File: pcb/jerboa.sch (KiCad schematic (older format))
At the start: 11 parts, among them P101 SWD_TC, U101 STM32L051K8U6

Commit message: Some schematic work, create a todo with ideas for power supply components
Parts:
- added R?: 1M, agg:0402, symbol agg-kicad:R
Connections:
- net GND: now also R?.2
- net MCU_SHUTDOWN_TO_RADIO: now also R?.1
- net GPS_~RESET: now reaches U101.28 (PB5)
- no-connect marks 17 -> 16
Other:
- moved on the sheet: C101, C102, C103, C104, C105, C106, C107, D101, P101, R101, U101

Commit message: Add TPS61025 switching regulator to schematic
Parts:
- C102, C104, C105, C106, C107: Farnell 2496810 -> 1288282
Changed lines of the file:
@@
 F 2 "agg:0402" H 4250 2200 50  0001 C CNN
 F 3 "" H 4250 2200 50  0001 C CNN
-F 4 "2496810" H 4250 2200 60  0001 C CNN "Farnell"
+F 4 "1288282" H 4250 2200 60  0001 C CNN "Farnell"
 	1    4250 2200
 	1    0    0    -1
@@
 F 2 "agg:0402" H 4050 2400 50  0001 C CNN
 F 3 "" H 4050 2400 50  0001 C CNN
-F 4 "2496810" H 4050 2400 60  0001 C CNN "Farnell"
+F 4 "1288282" H 4050 2400 60  0001 C CNN "Farnell"
 	1    4050 2400
 	1    0    0    -1
@@
 F 2 "agg:0402" H 4250 2600 50  0001 C CNN
 F 3 "" H 4250 2600 50  0001 C CNN
-F 4 "2496810" H 4250 2600 60  0001 C CNN "Farnell"
+F 4 "1288282" H 4250 2600 60  0001 C CNN "Farnell"
 	1    4250 2600
 	1    0    0    -1
@@
 F 2 "agg:0402" H 4700 2750 50  0001 C CNN
 F 3 "" H 4700 2750 50  0001 C CNN
-F 4 "2496810" H 4700 2750 60  0001 C CNN "Farnell"
+F 4 "1288282" H 4700 2750 60  0001 C CNN "Farnell"
 	1    4700 2750
 	0    1    1    0
@@
 F 2 "agg:0402" H 5000 5950 50  0001 C CNN
 F 3 "" H 5000 5950 50  0001 C CNN
-F 4 "2496810" H 5000 5950 60  0001 C CNN "Farnell"
+F 4 "1288282" H 5000 5950 60  0001 C CNN "Farnell"
 	1    5000 5950
 	0    -1   -1   0

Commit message: Create some more schematic symbols and footprints
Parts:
- added IC?: SL18860DC, agg:DFN-10-SL18860DC, symbol agg-kicad:SL18860DC
- added Y?: TCXO, Jerboa:2x1.6mm_TCXO, symbol agg-kicad:TCXO
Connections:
- no-connect marks 16 -> 15
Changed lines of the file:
@@
 	4050 2400 4000 2400
 Wire Wire Line
-	4000 2000 4000 2200
+	4000 2000 4000 2850
 Connection ~ 4000 2600
 Wire Wire Line
@@
 	4400 2800 4150 2800
 Wire Wire Line
-	4400 1900 4400 2000
+	4400 1900 4400 2800
 Connection ~ 4400 2600
 Wire Wire Line
@@
 	4400 2300 5000 2300
 Wire Wire Line
-	4150 2400 4400 2400
+	4150 2400 5000 2400
 Wire Wire Line
 	4400 2500 5000 2500
@@
 NRST
 Wire Wire Line
-	4650 2700 4700 2700
+	4650 2700 5000 2700
 Text Label 6850 4800 0    60   ~ 0
 TX_GPS_from_MCU
@@
 Wire Wire Line
 	6700 4900 6850 4900
-NoConn ~ 5000 3100
 NoConn ~ 5000 3200
 NoConn ~ 6700 2300
@@
 NoConn ~ 6700 5100
 Wire Wire Line
-	5000 6000 5400 6000
-Wire Wire Line
-	5000 5800 5400 5800
+	5000 6000 5500 6000
+Wire Wire Line
+	5000 5800 5500 5800
 Text Label 1600 6150 0    60   ~ 0
 MCU_NSS_TO_RADIO
@@
 MCU_nIRQ_TO_RADIO
 Wire Wire Line
-	4000 2600 4000 2800
-Wire Wire Line
-	4000 2400 4000 2600
-Wire Wire Line
-	4000 2200 4000 2400
-Wire Wire Line
-	4000 2800 4000 2850
-Wire Wire Line
-	4400 2600 4400 2800
-Wire Wire Line
-	4400 2200 4400 2300
-Wire Wire Line
-	4400 2000 4400 2200
-Wire Wire Line
-	4400 2300 4400 2400
-Wire Wire Line
-	4400 2400 5000 2400
-Wire Wire Line
-	4400 2400 4400 2500
-Wire Wire Line
-	4400 2500 4400 2600
-Wire Wire Line
-	5400 5800 5500 5800
-Wire Wire Line
-	5400 6000 5500 6000
-Wire Wire Line
-	4700 2700 5000 2700
-Wire Wire Line
 	6850 4800 6700 4800
 $Comp
@@
 	8100 2700 8100 2650
 Wire Wire Line
-	6700 2500 8100 2500
+	6700 2500 8300 2500
 Wire Wire Line
 	8100 2550 8100 2500
 Connection ~ 8100 2500
-Wire Wire Line
-	8100 2500 8300 2500
 Wire Wire Line
 	1400 3700 1600 3700
@@
 Wire Wire Line
 	6850 4700 6700 4700
+$Comp
+L agg-kicad:SL18860DC IC?
+U 1 1 5A7CC280
+P 3250 4450
+F 0 "IC?" H 3250 5075 50  0000 C CNN
+F 1 "SL18860DC" H 3250 4984 50  0000 C CNN
+F 2 "agg:DFN-10-SL18860DC" H 2850 3850 50  0001 L CNN
+F 3 "http://www.silabs.com/Support%20Documents/TechnicalDocs/SL18860.pdf" H 2850 3750 50  0001 L CNN
+F 4 "634-SL18860DC" H 2850 3650 50  0001 L CNN "Mouser"
+	1    3250 4450
+	1    0    0    -1
+$EndComp
+$Comp
+L agg-kicad:TCXO Y?
+U 1 1 5A7E3BDC
+P 2250 4500
+F 0 "Y?" H 2250 4725 50  0000 C CNN
+F 1 "TCXO" H 2250 4634 50  0000 C CNN
+F 2 "Jerboa:2x1.6mm_TCXO" H 2050 4500 50  0001 C CNN
+F 3 "http://www.farnell.com/datasheets/2045487.pdf" H 2050 4500 50  0001 C CNN
+F 4 "2545847" H 2050 4200 50  0001 L CNN "Farnell"
+	1    2250 4500
+	1    0    0    -1
+$EndComp
 $EndSCHEMATC

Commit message: Work on schematic
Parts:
- added C? (x2): 100nF, agg:0402, symbol agg-kicad:C
- added C?: 10uF, agg:0402, symbol agg-kicad:C
- added R? (x2): 10k, symbol agg-kicad:R
- added R?: 50, symbol agg-kicad:R
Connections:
- net 3v3: now also IC?.6 (OE1), IC?.7 (OE2), Y?.4 (VCC), C?.2, R?.1
- net GND: now also IC?.1 (VSS), IC?.5 (OE3), Y?.2 (GND), C?.1, C?.1, C?.1, R?.2
- net MCU_CLK: now reaches U101.2 (PC14-OSC_IN)
- net MCU_CLK: now also IC?.8 (CLKOUT1)
- net at IC?.2 (VDD): now also C?.2, C?.2, R?.2
- net at IC?.3 (CLKIN): now also Y?.3 (OUT)
- net at IC?.9 (CLKOUT2): now also R?.1
- new net SI4460_CLK: R?.1, R?.2
- no-connect marks 15 -> 17
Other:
- note removed: "No DFU required"
- moved on the sheet: C101, C102, C103, C104, C105, C106, C107, D101, IC?, P101, R101, R?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

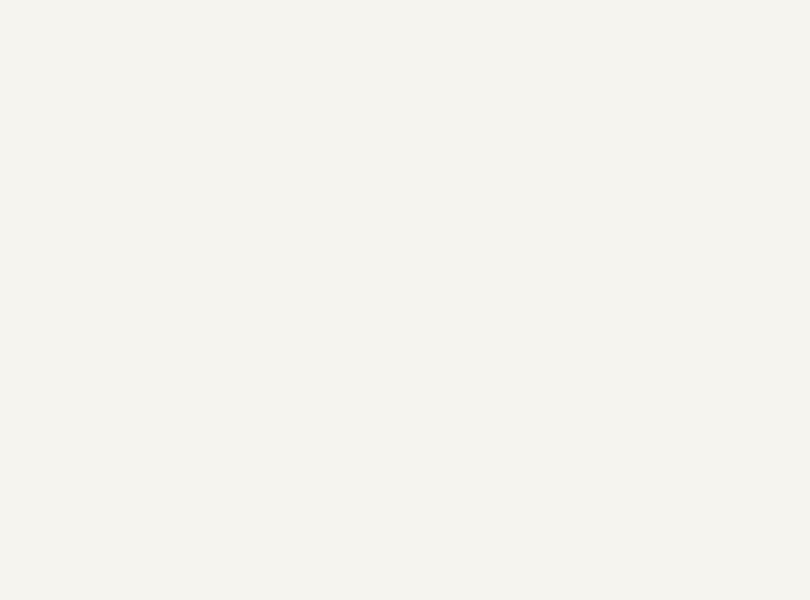
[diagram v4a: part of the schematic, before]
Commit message: Add wspr breakout board and reorganise sub project libraries
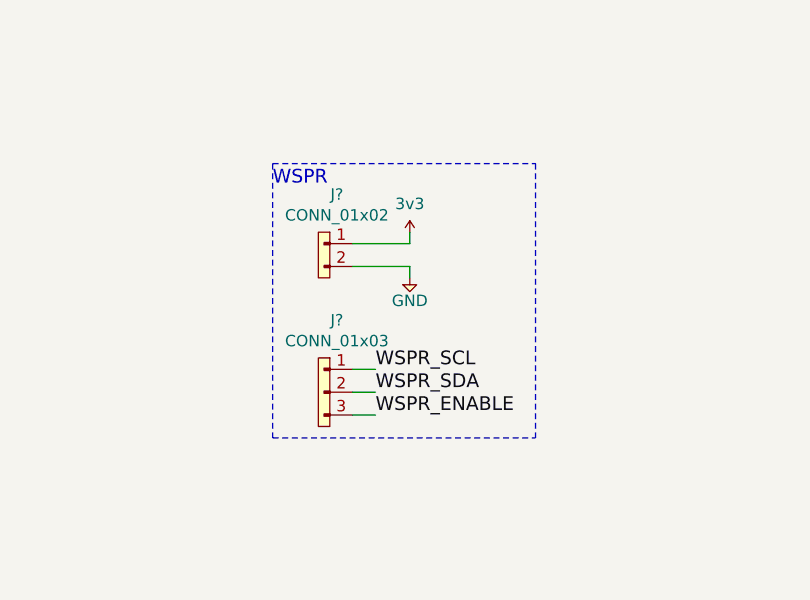
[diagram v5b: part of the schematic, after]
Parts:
- added J?: CONN_01x02, agg:SIL-254P-02, symbol agg-kicad:CONN_01x02
- added J?: CONN_01x03, symbol agg-kicad:CONN_01x03
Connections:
- net 3v3: now also J?.1
- net GND: now also J?.2
- new net WSPR_ENABLE: J?.3
- new net WSPR_SCL: J?.1
- new net WSPR_SDA: J?.2
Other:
- note added: "WSPR"
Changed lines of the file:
@@
 	3350 4100 3350 4050
 Connection ~ 3350 4250
+$Comp
+L agg-kicad:CONN_01x02 J?
+U 1 1 5A89E783
+P 3200 1750
+F 0 "J?" H 3231 1965 50  0000 C CNN
+F 1 "CONN_01x02" H 3231 1874 50  0000 C CNN
+F 2 "agg:SIL-254P-02" H 3200 1750 50  0001 C CNN
+F 3 "http://www.farnell.com/datasheets/2290158.pdf" H 3200 1750 50  0001 C CNN
+F 4 "1593458" H 3200 1750 50  0001 C CNN "Farnell"
+	1    3200 1750
+	1    0    0    -1
+$EndComp
+$Comp
+L agg-kicad:GND #PWR?
+U 1 1 5A89E908
+P 3550 1900
+F 0 "#PWR?" H 3420 1940 50  0001 L CNN
+F 1 "GND" H 3550 1800 50  0000 C CNN
+F 2 "" H 3550 1900 60  0001 C CNN
+F 3 "" H 3550 1900 60  0001 C CNN
+F 4 "Value" H 3550 1900 50  0001 C CNN "Farnell"
+	1    3550 1900
+	1    0    0    -1
+$EndComp
+$Comp
+L agg-kicad:3v3 #PWR?
+U 1 1 5A89EBB4
+P 3550 1700
+F 0 "#PWR?" H 3550 1810 50  0001 L CNN
+F 1 "3v3" H 3550 1824 50  0000 C CNN
+F 2 "" H 3550 1700 60  0001 C CNN
+F 3 "" H 3550 1700 60  0001 C CNN
+	1    3550 1700
+	1    0    0    -1
+$EndComp
+Wire Wire Line
+	3550 1900 3550 1850
+Wire Wire Line
+	3550 1850 3300 1850
+Wire Wire Line
+	3300 1750 3550 1750
+Wire Wire Line
+	3550 1750 3550 1700
+$Comp
+L agg-kicad:CONN_01x03 J?
+U 1 1 5A8A71F9
+P 3200 2300
+F 0 "J?" H 3231 2515 50  0000 C CNN
+F 1 "CONN_01x03" H 3231 2424 50  0000 C CNN
+F 2 "" H 3200 2300 50  0001 C CNN
+F 3 "" H 3200 2300 50  0001 C CNN
+	1    3200 2300
+	1    0    0    -1
+$EndComp
+Text Label 3400 2300 0    60   ~ 0
+WSPR_SCL
+Text Label 3400 2400 0    60   ~ 0
+WSPR_SDA
+Text Label 3400 2500 0    60   ~ 0
+WSPR_ENABLE
+Wire Wire Line
+	3400 2300 3300 2300
+Wire Wire Line
+	3300 2400 3400 2400
+Wire Wire Line
+	3300 2500 3400 2500
+Text Notes 2950 1500 0    60   ~ 0
+WSPR
+Wire Notes Line
+	2950 1400 2950 2600
+Wire Notes Line
+	2950 2600 4100 2600
+Wire Notes Line
+	2950 1400 4100 1400
+Wire Notes Line
+	4100 1400 4100 2600
 $EndSCHEMATC

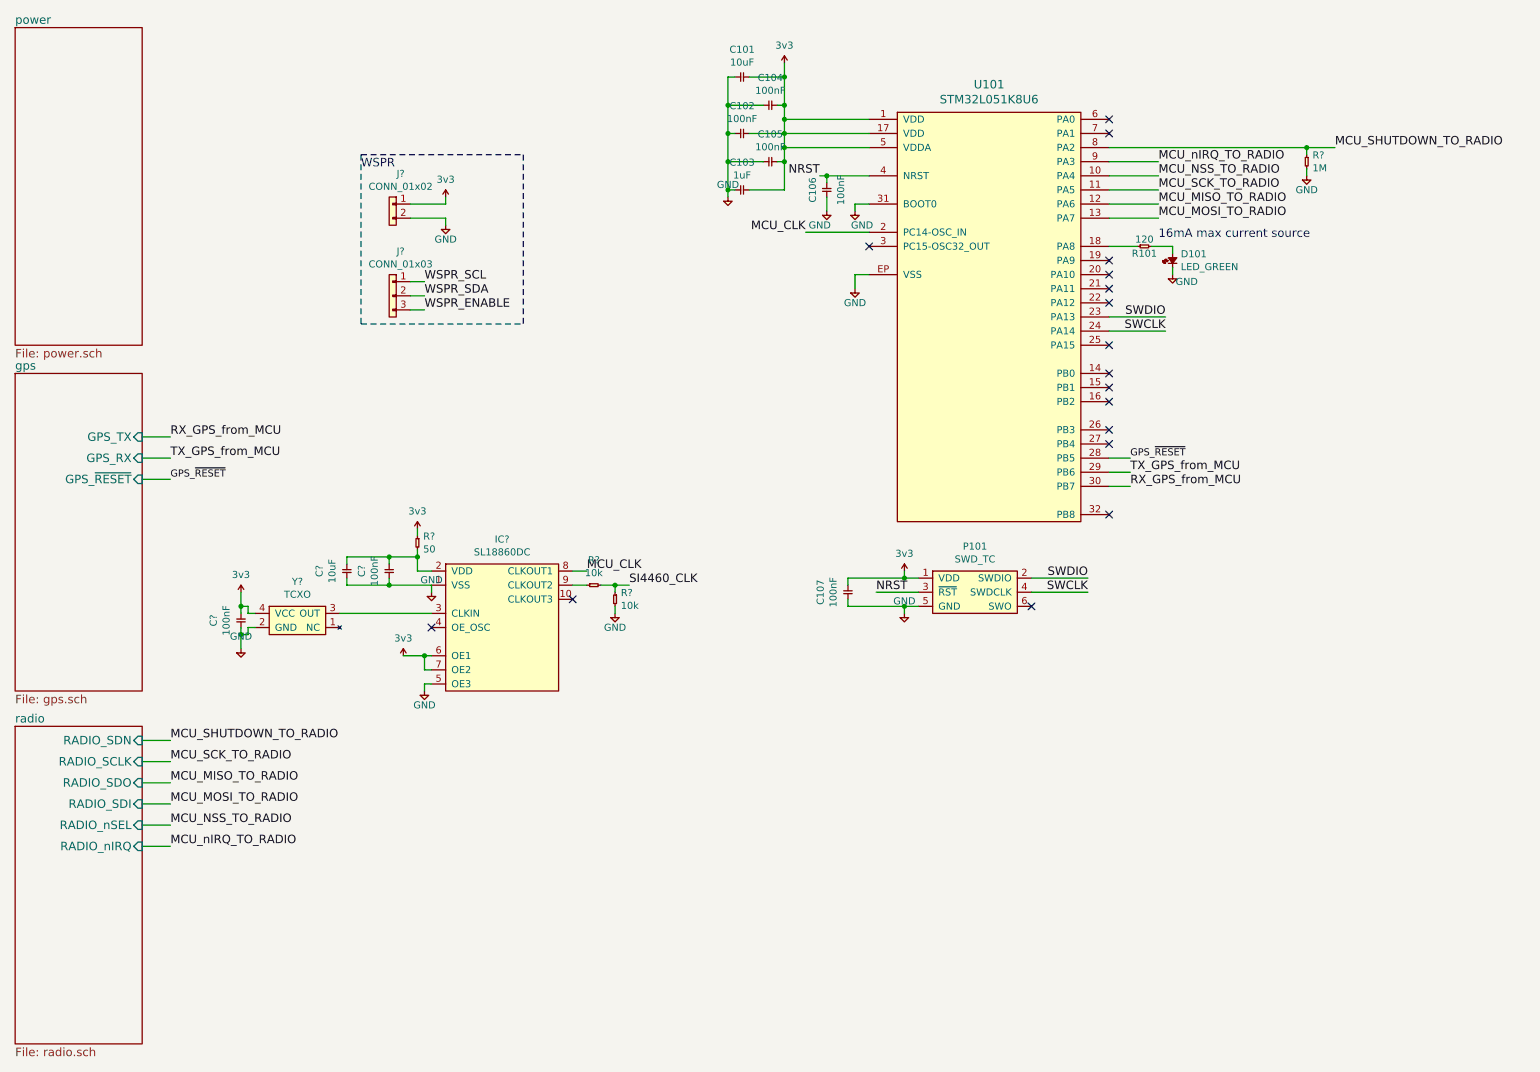
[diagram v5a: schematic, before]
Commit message: Update clock input for clock buffer
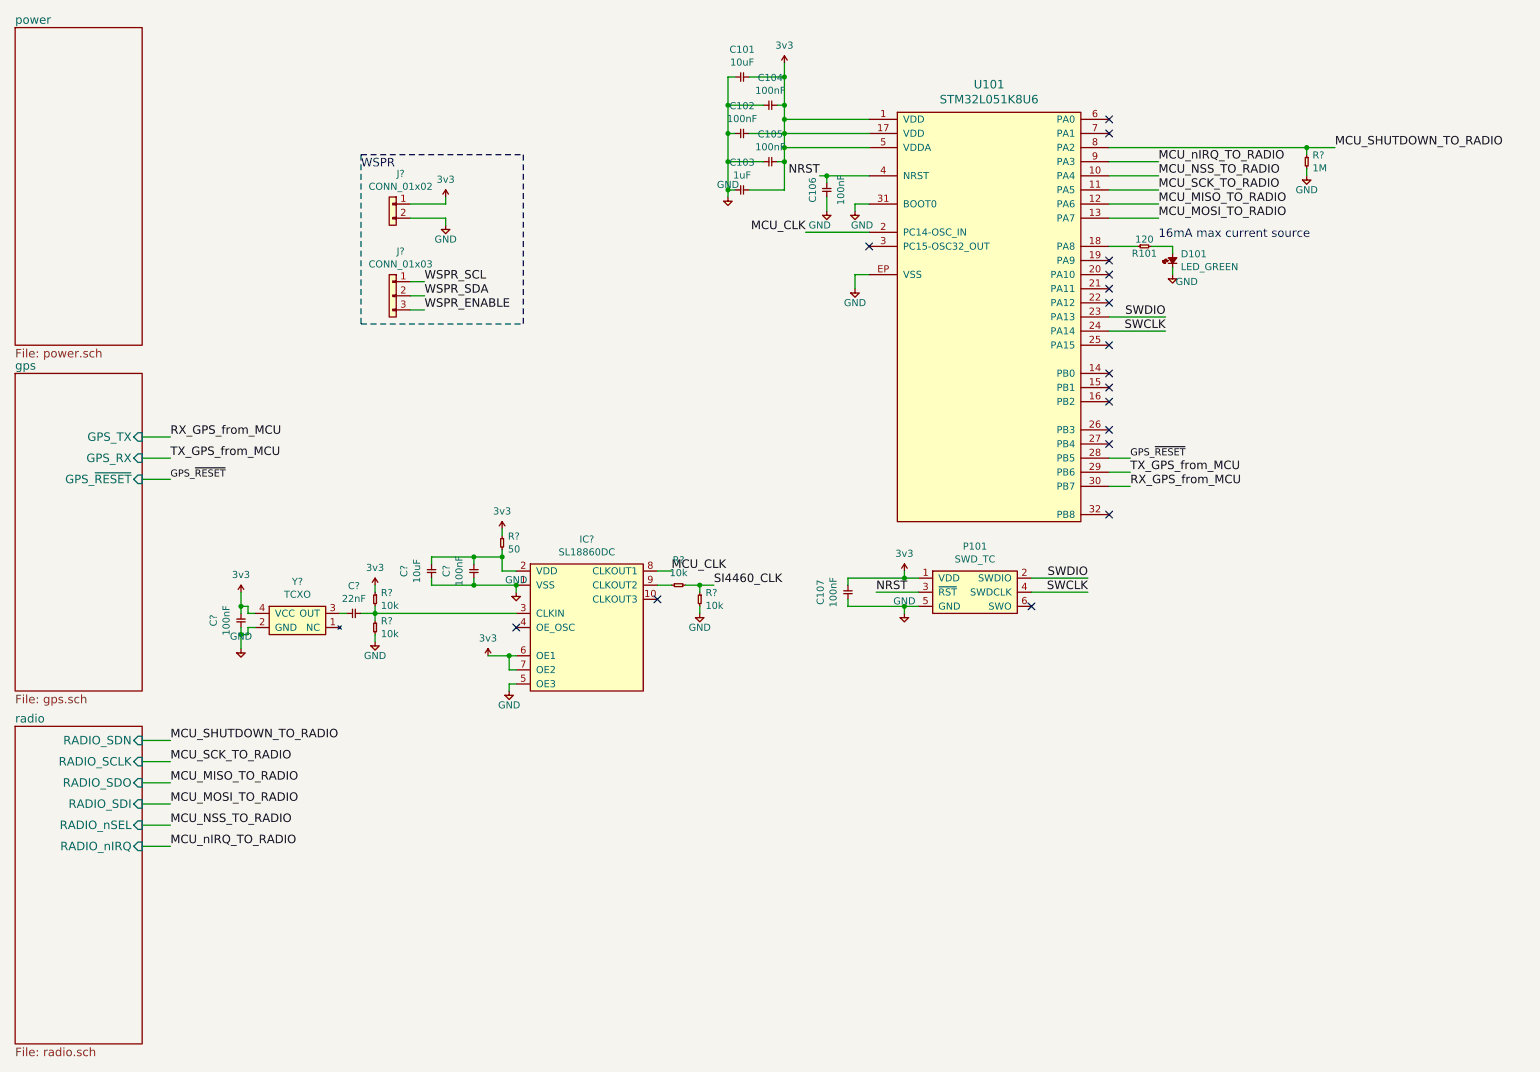
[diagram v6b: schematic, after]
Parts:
- added C?: 22nF, agg:0402, symbol agg-kicad:C
- added R? (x2): 10k, symbol agg-kicad:R
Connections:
- net 3v3: now also R?.1
- net GND: now also R?.2
- net at IC?.3 (CLKIN): now also C?.2, R?.1, R?.2; no longer Y?.3 (OUT)
- new net: C?.1, Y?.3 (OUT)
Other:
- moved on the sheet: C?, IC?, R?
